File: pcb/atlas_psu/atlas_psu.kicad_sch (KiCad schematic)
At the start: 68 parts, among them J1 SECONDARY_AC, J2 NORMAL_SOURCE, J3 SYSTEM_FEED, J4 ANALOG_POWER, J5 STACK_POWER, J6 PSU_STATUS, J7 CHASSIS_CONTACT, U1 LM317T, U2 LM337T, U3 LM317T, U4 TL431BIDBZR, U5 TL431BIDBZR, U6 TL431BIDBZR, U7 LTV-817S-TA1-D, U8 LTV-817S-TA1-D, U9 LTV-817S-TA1-D

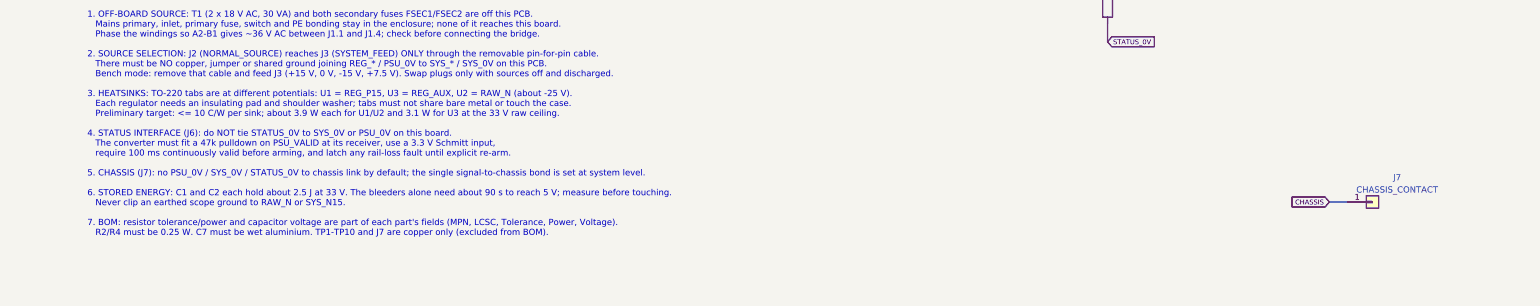
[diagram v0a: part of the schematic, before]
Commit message: Reconcile PSU prototype and publish validation studies
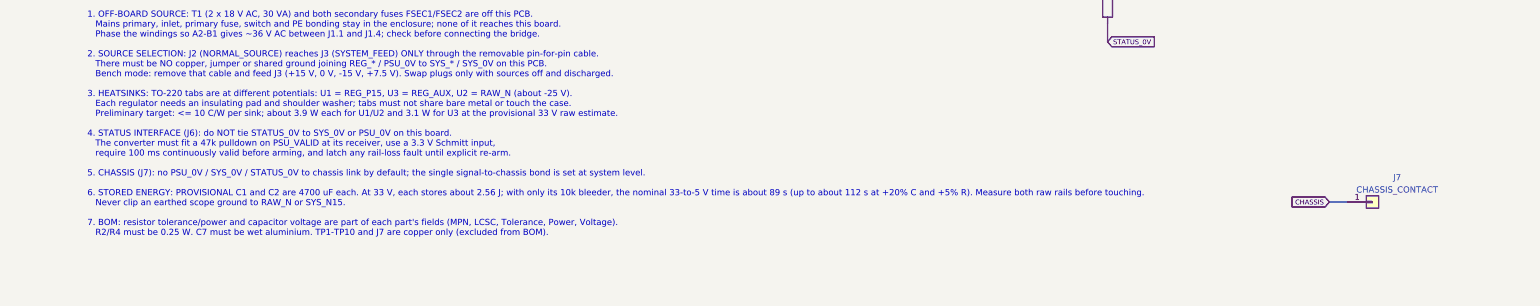
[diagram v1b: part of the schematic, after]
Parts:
- C1, C2: Note 105 C aluminium snap-in; verify 100 Hz ripple current/life -> PROVISIONAL 105 C snap-in, 30x30 mm, 10 mm pitch; 2.1 A rms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
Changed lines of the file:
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@@
 		(date "2026-09-24")
 		(rev "A")
-		(comment 1 "Design reference: pcb/atlas_psu/PSU_DESIGN_PLAN.md")
+		(comment 1 "Design reference: BOTS/PLANS/PSU_DESIGN_PLAN.md")
 		(comment 2 "Net allocation verified against plan section 3.9")
 	)
@@
 			)
 		)
-		(property "Datasheet" ""
+		(property "Datasheet" "https://www.nichicon.com/getmedia/6716b3c6-abcc-4da1-80b0-b33e29e5a195/e-lgy-DB.pdf"
 			(at 38.1 68.58 0)
 			(hide yes)
@@
 		(property "Tolerance" "20%" (at 38.1 68.58 0) (hide yes) (effects (font (size 1.27 1.27))))
 		(property "Voltage" "50V" (at 38.1 68.58 0) (hide yes) (effects (font (size 1.27 1.27))))
-		(property "Note" "105 C aluminium snap-in; verify 100 Hz ripple current/life" (at 38.1 68.58 0) (hide yes) (effects (font (size 1.27 1.27))))
+		(property "Note" "PROVISIONAL 105 C snap-in, 30x30 mm, 10 mm pitch; 2.1 A rms at 120 Hz; qualify capacitor RMS current and inrush" (at 38.1 68.58 0) (hide yes) (effects (font (size 1.27 1.27))))
 		(pin "1"
 		)
@@
 			)
 		)
-		(property "Datasheet" ""
+		(property "Datasheet" "https://www.nichicon.com/getmedia/6716b3c6-abcc-4da1-80b0-b33e29e5a195/e-lgy-DB.pdf"
 			(at 72.39 68.58 0)
 			(hide yes)
@@
 		(property "Tolerance" "20%" (at 72.39 68.58 0) (hide yes) (effects (font (size 1.27 1.27))))
 		(property "Voltage" "50V" (at 72.39 68.58 0) (hide yes) (effects (font (size 1.27 1.27))))
-		(property "Note" "105 C aluminium snap-in; verify 100 Hz ripple current/life" (at 72.39 68.58 0) (hide yes) (effects (font (size 1.27 1.27))))
+		(property "Note" "PROVISIONAL 105 C snap-in, 30x30 mm, 10 mm pitch; 2.1 A rms at 120 Hz; qualify capacitor RMS current and inrush" (at 72.39 68.58 0) (hide yes) (effects (font (size 1.27 1.27))))
 		(pin "1"
 		)
@@
 		)
 	)
-	(text "1. OFF-BOARD SOURCE: T1 (2 x 18 V AC, 30 VA) and both secondary fuses FSEC1/FSEC2 are off this PCB.\n   Mains primary, inlet, primary fuse, switch and PE bonding stay in the enclosure; none of it reaches this board.\n   Phase the windings so A2-B1 gives ~36 V AC between J1.1 and J1.4; check before connecting the bridge.\n\n2. SOURCE SELECTION: J2 (NORMAL_SOURCE) reaches J3 (SYSTEM_FEED) ONLY through the removable pin-for-pin cable.\n   There must be NO copper, jumper or shared ground joining REG_* / PSU_0V to SYS_* / SYS_0V on this PCB.\n   Bench mode: remove that cable and feed J3 (+15 V, 0 V, -15 V, +7.5 V). Swap plugs only with sources off and discharged.\n\n3. HEATSINKS: TO-220 tabs are at different potentials: U1 = REG_P15, U3 = REG_AUX, U2 = RAW_N (about -25 V).\n   Each regulator needs an insulating pad and shoulder washer; tabs must not share bare metal or touch the case.\n   Preliminary target: <= 10 C/W per sink; about 3.9 W each for U1/U2 and 3.1 W for U3 at the 33 V raw ceiling.\n\n4. STATUS INTERFACE (J6): do NOT tie STATUS_0V to SYS_0V or PSU_0V on this board.\n   The converter must fit a 47k pulldown on PSU_VALID at its receiver, use a 3.3 V Schmitt input,\n   require 100 ms continuously valid before arming, and latch any rail-loss fault until explicit re-arm.\n\n5. CHASSIS (J7): no PSU_0V / SYS_0V / STATUS_0V to chassis link by default; the single signal-to-chassis bond is set at system level.\n\n6. STORED ENERGY: C1 and C2 each hold about 2.5 J at 33 V. The bleeders alone need about 90 s to reach 5 V; measure before touching.\n   Never clip an earthed scope ground to RAW_N or SYS_N15.\n\n7. BOM: resistor tolerance/power and capacitor voltage are part of each part's fields (MPN, LCSC, Tolerance, Power, Voltage).\n   R2/R4 must be 0.25 W. C7 must be wet aluminium. TP1-TP10 and J7 are copper only (excluded from BOM)."
+	(text "1. OFF-BOARD SOURCE: T1 (2 x 18 V AC, 30 VA) and both secondary fuses FSEC1/FSEC2 are off this PCB.\n   Mains primary, inlet, primary fuse, switch and PE bonding stay in the enclosure; none of it reaches this board.\n   Phase the windings so A2-B1 gives ~36 V AC between J1.1 and J1.4; check before connecting the bridge.\n\n2. SOURCE SELECTION: J2 (NORMAL_SOURCE) reaches J3 (SYSTEM_FEED) ONLY through the removable pin-for-pin cable.\n   There must be NO copper, jumper or shared ground joining REG_* / PSU_0V to SYS_* / SYS_0V on this PCB.\n   Bench mode: remove that cable and feed J3 (+15 V, 0 V, -15 V, +7.5 V). Swap plugs only with sources off and discharged.\n\n3. HEATSINKS: TO-220 tabs are at different potentials: U1 = REG_P15, U3 = REG_AUX, U2 = RAW_N (about -25 V).\n   Each regulator needs an insulating pad and shoulder washer; tabs must not share bare metal or touch the case.\n   Preliminary target: <= 10 C/W per sink; about 3.9 W each for U1/U2 and 3.1 W for U3 at the provisional 33 V raw estimate.\n\n4. STATUS INTERFACE (J6): do NOT tie STATUS_0V to SYS_0V or PSU_0V on this board.\n   The converter must fit a 47k pulldown on PSU_VALID at its receiver, use a 3.3 V Schmitt input,\n   require 100 ms continuously valid before arming, and latch any rail-loss fault until explicit re-arm.\n\n5. CHASSIS (J7): no PSU_0V / SYS_0V / STATUS_0V to chassis link by default; the single signal-to-chassis bond is set at system level.\n\n6. STORED ENERGY: PROVISIONAL C1 and C2 are 4700 uF each. At 33 V, each stores about 2.56 J; with only its 10k bleeder, the nominal 33-to-5 V time is about 89 s (up to about 112 s at +20% C and +5% R). Measure both raw rails before touching.\n   Never clip an earthed scope ground to RAW_N or SYS_N15.\n\n7. BOM: resistor tolerance/power and capacitor voltage are part of each part's fields (MPN, LCSC, Tolerance, Power, Voltage).\n   R2/R4 must be 0.25 W. C7 must be wet aluminium. TP1-TP10 and J7 are copper only (excluded from BOM)."
 		(exclude_from_sim no)
 		(at 285 296 0)
